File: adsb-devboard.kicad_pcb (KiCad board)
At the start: 4 copper layers, 52.4 x 35.7 mm, 89 parts, among them J1 USB_C_Receptacle_USB2.0_16P, J2 Conn_01x20_Pin, J3 Conn_01x20_Pin, J4 Conn_Coaxial, SW1 SW_Push, U1 ICE40UP5K-SG48ITR, U2 RP2350A-QFN60, U3 W25Q128JVP, U4 RT8075ZQW, U5 TJ-S1608SW6TDSLCCYRGB-A5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

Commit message: everything seems ready
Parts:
- C1, C2: value 15p -> 33p
- FB1, FB2, FB3: footprint Inductor_SMD:L_0402_1005Metric -> Inductor_SMD:L_0603_1608Metric
- R23: footprint Resistor_SMD:R_0402_1005Metric -> Resistor_SMD:R_0603_1608Metric
- moved FB1 1.27 mm to (145.7, 59.9)
- moved FB3 0.82 mm to (162.1, 61.2)
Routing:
- net 3v3_RF: track 28.8 -> 31.1 mm
- net 3v3: track 100.1 -> 101.0 mm

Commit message: sch cleanup and little upgrade
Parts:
- added C32: 4.7u, Capacitor_SMD:C_0402_1005Metric, F.Cu at (135.8, 68.1)
- added C33: 100n, Capacitor_SMD:C_0402_1005Metric, F.Cu at (134.8, 68.1)
- added C34: 4.7u, Capacitor_SMD:C_0402_1005Metric, F.Cu at (148.8, 66.9)
- added C35: 100n, Capacitor_SMD:C_0402_1005Metric, F.Cu at (150.8, 66.9)
- added C36: 4.7u, Capacitor_SMD:C_0402_1005Metric, F.Cu at (134.7, 70.3)
- added C37: 100n, Capacitor_SMD:C_0402_1005Metric, F.Cu at (133.7, 70.3)
- added C38: 4.7u, Capacitor_SMD:C_0402_1005Metric, F.Cu at (150.4, 63.8)
- added C39: 10u, Capacitor_SMD:C_0402_1005Metric, F.Cu at (150.4, 62.8)
- added C40: 4.7u, Capacitor_SMD:C_0402_1005Metric, F.Cu at (133.7, 72.9)
- added C41: 100n, Capacitor_SMD:C_0402_1005Metric, F.Cu at (134.4, 74.8)
- added C42: 4.7u, Capacitor_SMD:C_0402_1005Metric, F.Cu at (135.1, 79.8)
- added C43: 100n, Capacitor_SMD:C_0402_1005Metric, F.Cu at (134.3, 80.9)
- added C44: 4.7u, Capacitor_SMD:C_0402_1005Metric, F.Cu at (147.9, 61.5)
- added C45: 100n, Capacitor_SMD:C_0402_1005Metric, F.Cu at (147.9, 63.3)
- added R24: 100, Resistor_SMD:R_0402_1005Metric, F.Cu at (146.4, 63.4)
- added X2: TA0970B, easyeda2kicad:FILTER-SMD_6P-L3.8-W3.8-P1.27-TL-3, F.Cu at (174.5, 58.4)
- moved J4 8.78 mm to (181.4, 58.4)
- moved C23 3.10 mm to (144.3, 66.5)
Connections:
- C31 pad 2: /smaconn -> /firstsawout
- U1 pad 29: 1v2 -> Net-(U1D-VCCPLL)
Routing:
- net 1v2: track 73.9 -> 105.6 mm, vias 6 -> 9
- net 3v3: track 101.0 -> 128.1 mm, vias 27 -> 30
- net GND: track 46.2 -> 66.9 mm, vias 55 -> 59
- net Net-(U1D-VCCPLL): track 0.00 -> 14.5 mm, vias 0 -> 3
- net /firstsawout: track 0.00 -> 5.25 mm
- net /IO6: track 12.9 -> 13.5 mm

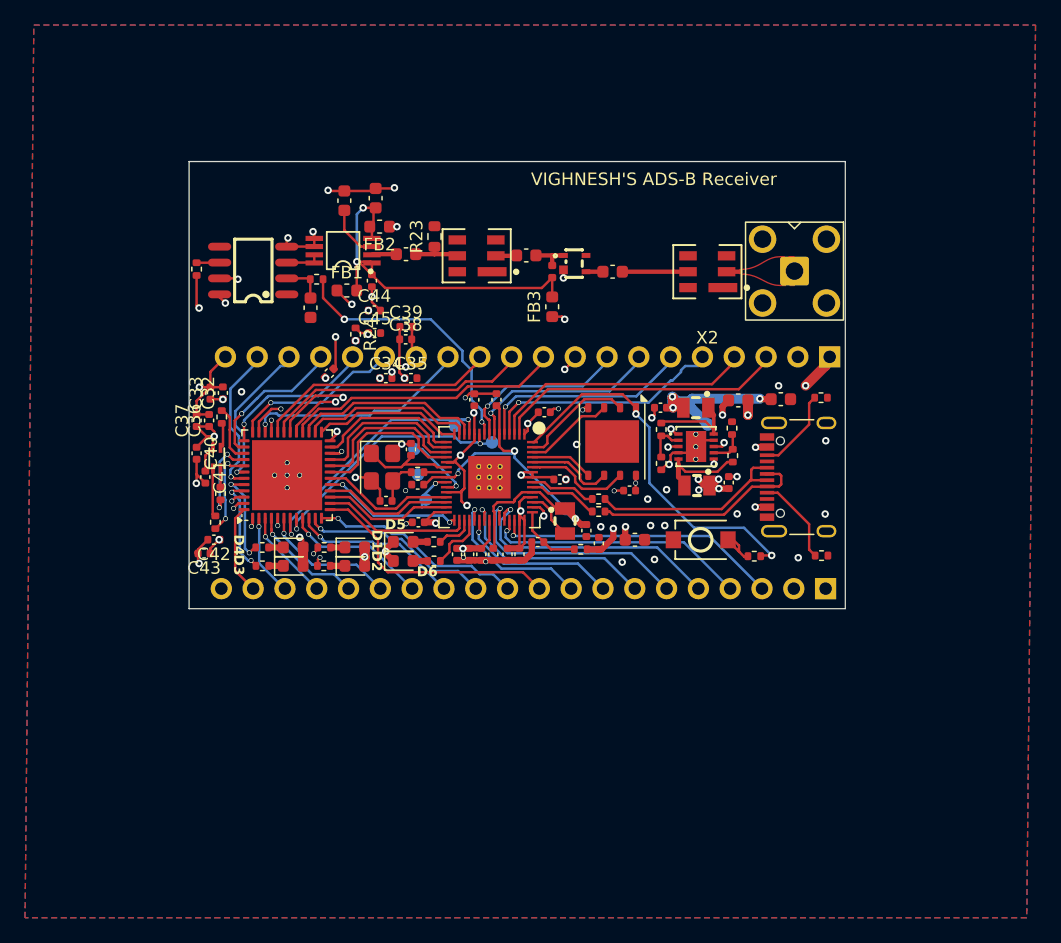
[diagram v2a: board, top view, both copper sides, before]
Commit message: rerouted rf
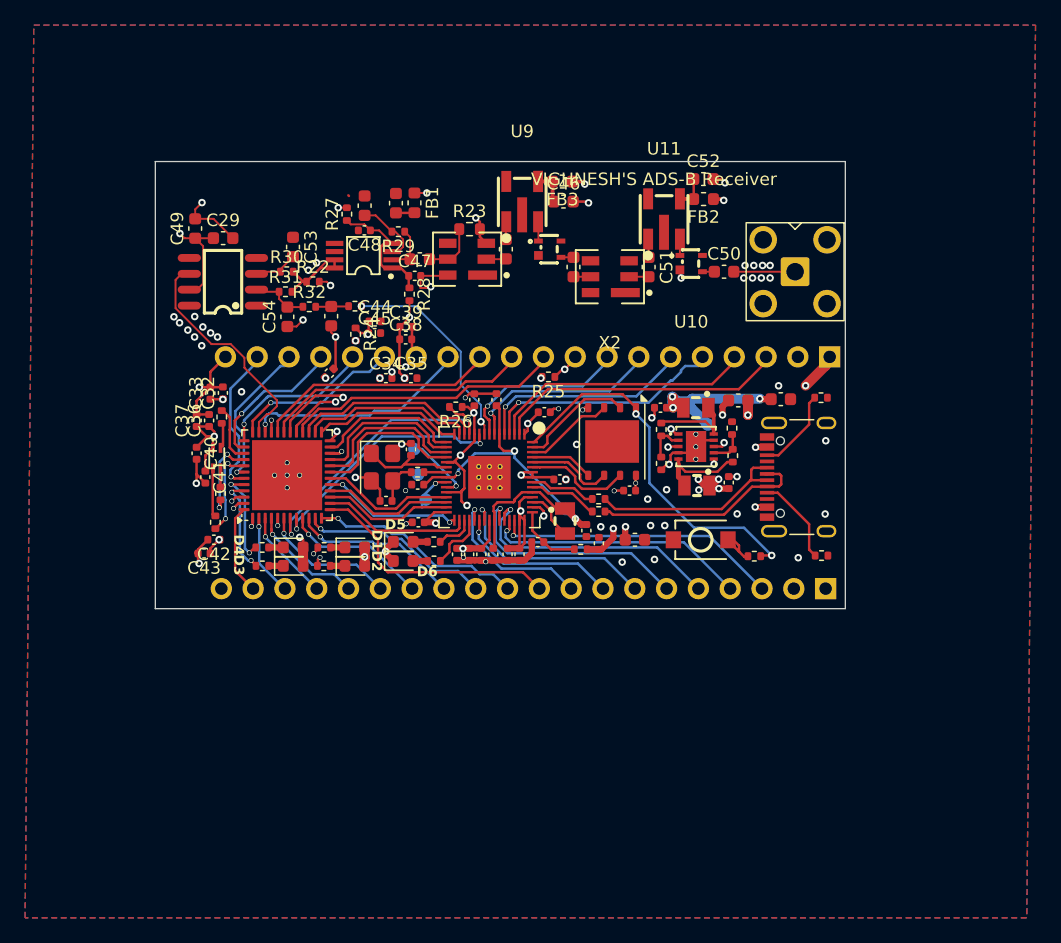
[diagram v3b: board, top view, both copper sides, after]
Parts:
- removed L4: 470nH, Inductor_SMD:L_0402_1005Metric
- removed TP5, TP6: TestPoint_Alt, TestPoint:TestPoint_Pad_D1.0mm
- added C46: 1500p, Capacitor_SMD:C_0603_1608Metric, F.Cu at (163.0, 52.8)
- added C47: 100n, Capacitor_SMD:C_0402_1005Metric, F.Cu at (151.1, 58.7)
- added C48: 100n, Capacitor_SMD:C_0402_1005Metric, F.Cu at (147.1, 55.1)
- added C49: 2.2u, Capacitor_SMD:C_0603_1608Metric, F.Cu at (133.6, 55.0)
- added C50: 1000p, Capacitor_SMD:C_0603_1608Metric, F.Cu at (175.8, 58.4)
- added C51: 100p, Capacitor_SMD:C_0603_1608Metric, F.Cu at (169.8, 58.0)
- added C52: 1500pf, Capacitor_SMD:C_0603_1608Metric, F.Cu at (174.2, 51.0)
- added C53: 3p, Capacitor_SMD:C_0603_1608Metric, F.Cu at (141.4, 56.4)
- added C54: 200p, Capacitor_SMD:C_0603_1608Metric, F.Cu at (140.9, 62.0)
- added R25: 10K, Resistor_SMD:R_0402_1005Metric, F.Cu at (161.8, 66.8)
- added R26: 2.2K, Resistor_SMD:R_0402_1005Metric, F.Cu at (154.4, 69.2)
- added R27: 100, Resistor_SMD:R_0402_1005Metric, F.Cu at (145.7, 53.8)
- added R28: 100, Resistor_SMD:R_0402_1005Metric, F.Cu at (150.7, 60.2)
- added R29: 53.6, Resistor_SMD:R_0402_1005Metric, F.Cu at (149.8, 55.2)
- added R30: 1K, Resistor_SMD:R_0402_1005Metric, F.Cu at (140.9, 58.4)
- added R31: 10K, Resistor_SMD:R_0402_1005Metric, F.Cu at (140.8, 60.0)
- added R32: 100K, Resistor_SMD:R_0402_1005Metric, F.Cu at (142.7, 61.2)
- added U10: SPF5189Z, easyeda2kicad:SOT-343-4_L2.0-W1.3-P1.30-LS2.1-BR, F.Cu at (173.2, 57.8)
- added U11: TCBT-14+, easyeda2kicad:SMD_L3.8-W3.8_TCBT-14, F.Cu at (171.0, 54.2)
- added U9: TCBT-14+, easyeda2kicad:SMD_L3.8-W3.8_TCBT-14, F.Cu at (159.7, 52.8)
- C26, C28: value 100p -> 680p
- C29: footprint Capacitor_SMD:C_0402_1005Metric -> Capacitor_SMD:C_0603_1608Metric
- C30: value 1u -> 100n
- C31: value 100p -> 1000p
- R22: value 330 -> 1K
- moved FB2 26.0 mm to (174.2, 52.6)
- moved C29 12.4 mm to (135.8, 55.7), turned to 0 degrees
- moved FB3 10.0 mm to (162.9, 51.2), turned to 180 degrees
- moved R22 9.34 mm to (143.0, 59.2), turned to 0 degrees
- moved FB1 8.84 mm to (151.1, 52.9), turned to -90 degrees
- moved X2 7.80 mm to (166.7, 58.8)
- moved R8 3.74 mm to (146.3, 61.1)
- moved C31 3.15 mm to (163.8, 58.0), turned to -90 degrees
- moved R23 2.86 mm to (155.5, 55.0), turned to 0 degrees
- moved U8 2.58 mm to (135.8, 59.2)
- moved U6 2.31 mm to (161.9, 56.6)
- moved C30 1.78 mm to (144.4, 62.0)
- moved C27 1.70 mm to (158.4, 56.6), turned to -90 degrees
- moved C25 1.67 mm to (149.6, 52.9)
- moved C28 1.67 mm to (147.1, 53.1)
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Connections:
- C27 pad 1: Net-(C27-Pad1) -> Net-(U9-RF)
- C29 pad 1: 3v3_RF -> 3v3
- C30 pad 1: Net-(U8--) -> Net-(C30-Pad1)
- FB2 pad 2: 3v3_RF -> 3v3_RF_LNA1
- FB3 pad 2: 3v3_RF -> 3v3_RF_LNA
- R22 pad 1: Net-(R22-Pad1) -> /adout
- R22 pad 2: /IO5 -> 3v3
- R8 pad 1: Net-(U8--) -> Net-(C30-Pad1)
- U6 pad 1: Net-(C27-Pad1) -> /biastee
- U7 pad 1: 3v3_RF -> 3v3_RF_D
- U7 pad 4: 3v3_RF -> 3v3_RF_D
- U8 pad 3: /adout -> Net-(U8-+)
- U8 pad 6: Net-(R22-Pad1) -> /IO5
- X2 pad 2: /smaconn -> /lnaout1
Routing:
- net 3v3_RF: track 31.1 -> 1.49 mm, vias 2 -> 0
- net 3v3: track 128.1 -> 140.0 mm, vias 30 -> 33
- net 3v3_RF_D: track 0.00 -> 10.4 mm
- net CRESETN: track 20.9 -> 27.5 mm, vias 2 -> 3
- net /GP6: track 21.8 -> 16.8 mm
- net /adout: track 2.86 -> 7.68 mm
- net GND: track 66.9 -> 71.1 mm, vias 59 -> 68
- net /firstsawout: track 5.25 -> 1.36 mm
- net /smaconn: track 1.07 -> 4.90 mm
- net Net-(U8-+): track 0.00 -> 3.60 mm
- net Net-(C27-Pad1): track 3.00 -> 0.00 mm
- net 3v3_RF_LNA: track 0.00 -> 2.80 mm
- net 3v3_RF_LNA1: track 0.00 -> 2.71 mm
- net Net-(C30-Pad1): track 0.00 -> 2.65 mm
- net /IO5: track 16.5 -> 18.4 mm, vias 2 -> 0
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- removed copper zone on F.Cu, net /smaconn
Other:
- board size 52.4 x 35.7 mm -> 55.1 x 35.7 mm

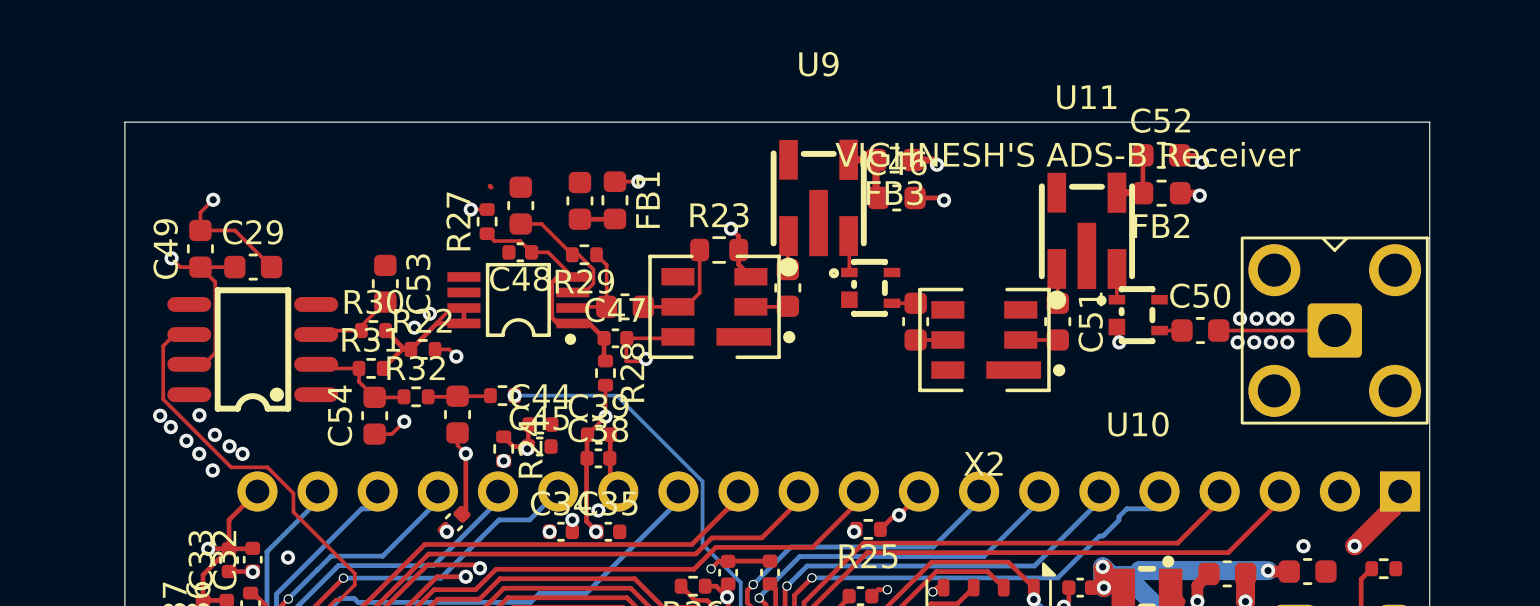
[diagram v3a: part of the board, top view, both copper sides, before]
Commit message: rerouted rf2
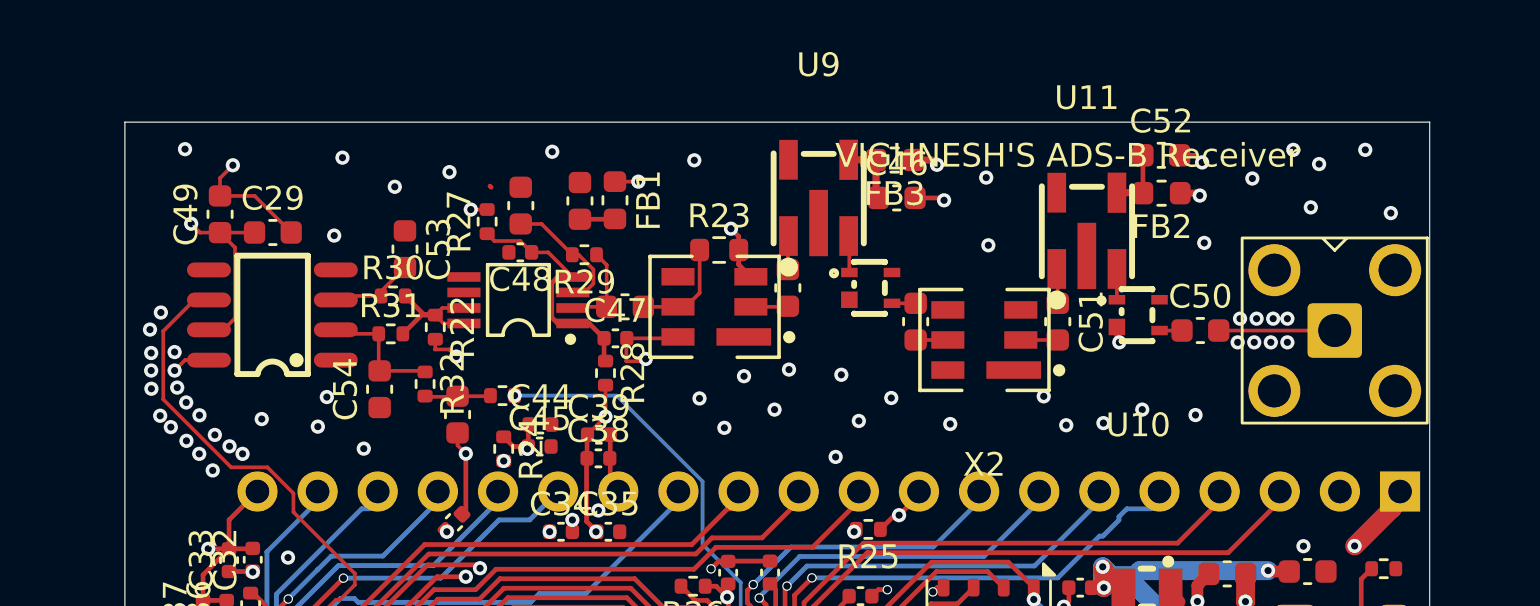
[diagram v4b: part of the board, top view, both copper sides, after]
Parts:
- moved C29 1.68 mm to (136.7, 54.3)
- moved C49 1.68 mm to (134.4, 53.5)
- moved R30 1.68 mm to (141.7, 56.9)
- moved R31 1.68 mm to (141.6, 58.5)
- moved U8 1.68 mm to (136.6, 57.7)
- moved C53 1.68 mm to (142.2, 55.0)
- moved C54 1.14 mm to (141.2, 60.9)
- moved R22 1.07 mm to (143.5, 58.3), turned to -90 degrees
- moved R32 0.66 mm to (143.1, 60.7), turned to -90 degrees
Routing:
- net /adout: track 7.68 -> 5.59 mm
- net /IO5: track 18.4 -> 20.2 mm
- net Net-(U8--): track 4.63 -> 5.40 mm
- net GND: track 71.1 -> 71.3 mm, vias 68 -> 109

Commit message: reeeerrouuuteed
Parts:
- removed R23: 51, Resistor_SMD:R_0603_1608Metric
- moved C28 14.0 mm to (133.5, 49.8)
- moved C48 14.0 mm to (133.5, 51.8)
- moved R29 14.0 mm to (136.2, 51.9)
- moved C25 14.0 mm to (136.0, 49.6)
- moved U7 14.0 mm to (133.4, 53.8)
- moved R27 14.0 mm to (132.1, 50.5)
- moved FB1 13.9 mm to (137.6, 49.6)
- moved C53 13.6 mm to (128.9, 57.7)
- moved C26 13.6 mm to (138.4, 54.1)
- moved X1 13.1 mm to (142.6, 54.1)
- moved C47 12.2 mm to (139.2, 56.4)
- moved R28 12.2 mm to (138.8, 57.9)
- moved R22 12.1 mm to (131.6, 56.5), turned to 0 degrees
- moved R30 11.6 mm to (130.2, 58.2), turned to 90 degrees
- moved C27 11.5 mm to (147.1, 54.2), turned to 180 degrees
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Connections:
- net /smaconn renamed /sma_connector
- C49 pad 1: 3v3 -> GND
- C49 pad 2: GND -> 3v3
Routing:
- net 3v3: track 140.4 -> 165.0 mm
- net /GP6: track 16.8 -> 28.2 mm, vias 2 -> 3
- net 3v3_RF_D: track 10.4 -> 20.0 mm, vias 0 -> 3
- net /IO5: track 20.2 -> 15.0 mm
- net 1v2: track 105.3 -> 109.0 mm
- net /sawout: track 4.62 -> 1.93 mm
- net Net-(U1D-VCCPLL): track 13.4 -> 15.4 mm
- net /lnaout1: track 1.56 -> 2.47 mm
- net GND: track 71.3 -> 72.0 mm, vias 109 -> 281
- net Net-(U7-INHI): track 3.83 -> 4.49 mm
- net /lnaout: track 1.57 -> 2.22 mm
- net (no net): vias 3 -> 13
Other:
- board size 55.1 x 35.7 mm -> 57.9 x 37.5 mm

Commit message: I HAVE ROUTED THIS FOR THE NTH TIME IDK I HAVE LOST COUNT
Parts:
- removed C27, C51: 100p, Capacitor_SMD:C_0603_1608Metric
- removed U11, U9: TCBT-14+, easyeda2kicad:SMD_L3.8-W3.8_TCBT-14
- removed U5: TJ-S1608SW6TDSLCCYRGB-A5, easyeda2kicad:LED-ARRAY-SMD_4P-L1.6-W0.8-BL-FD
- added H1: MountingHole, MountingHole:MountingHole_2.7mm_M2.5, F.Cu at (130.8, 77.9)
- added H3: MountingHole, MountingHole:MountingHole_2.7mm_M2.5, F.Cu at (182.3, 51.0)
- added L4: HP0603-R10H-N, easyeda2kicad:IND-SMD_L1.6-W1.0, F.Cu at (169.9, 54.5)
- added L5: HP0603-R10H-N, easyeda2kicad:IND-SMD_L1.6-W1.0, F.Cu at (158.0, 54.6)
- C31: footprint Capacitor_SMD:C_0603_1608Metric -> Capacitor_SMD:C_0402_1005Metric
- moved R29 11.4 mm to (147.5, 53.2)
- moved C26 11.3 mm to (149.6, 55.7)
- moved C28 11.3 mm to (144.7, 51.4)
- moved FB1 11.3 mm to (148.8, 51.2)
- moved X1 11.3 mm to (153.8, 55.7)
- moved C25 11.3 mm to (147.2, 51.2)
- moved R27 11.3 mm to (143.3, 52.1)
- moved U7 11.3 mm to (144.6, 55.4)
- moved C48 11.2 mm to (144.5, 53.5)
- moved C53 10.6 mm to (139.0, 54.2), turned to 180 degrees
- moved R22 8.70 mm to (140.3, 56.9), turned to -90 degrees
- moved R30 8.65 mm to (138.5, 55.6), turned to 0 degrees
- moved C47 8.22 mm to (147.3, 57.9)
- moved R28 8.14 mm to (146.8, 59.3)
- moved FB3 7.48 mm to (161.2, 54.5)
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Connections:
- X1 pad 2: /lnaout -> /biastee
- X2 pad 2: /lnaout1 -> /biastee1
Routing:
- net /IO5: track 15.0 -> 23.6 mm
- net /biastee1: track 1.74 -> 6.62 mm
- net 3v3: track 165.0 -> 160.6 mm
- net /biastee: track 1.33 -> 5.25 mm
- net 3v3_RF_D: track 20.0 -> 16.3 mm
- net /lnaout1: track 2.47 -> 0.00 mm
- net /lnaout: track 2.22 -> 0.00 mm
- net GND: track 72.0 -> 74.2 mm, vias 281 -> 279
- net Net-(U11-RF): track 1.91 -> 0.00 mm
- net Net-(U9-RF): track 1.73 -> 0.00 mm
- net Net-(U7-INLO): track 5.48 -> 6.33 mm
- net /GP6: track 28.2 -> 27.4 mm
- net 3v3_RF_LNA1: track 2.68 -> 3.43 mm
- net (no net): vias 13 -> 9
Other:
- board text removed: "D3"
- board text removed: "D4"
